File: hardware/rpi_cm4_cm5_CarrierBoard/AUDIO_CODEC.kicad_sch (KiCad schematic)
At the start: 33 parts, among them J12 SJ-3523-SMT-TR, J13 SJ-3523-SMT-TR, J14 SJ-3523-SMT-TR, U34 SGTL5000XNBA3R2, U35 AP22913W6-7, U36 AP22913W6-7, U37 12MHz, X1 CMM-3729AT-42308-TR

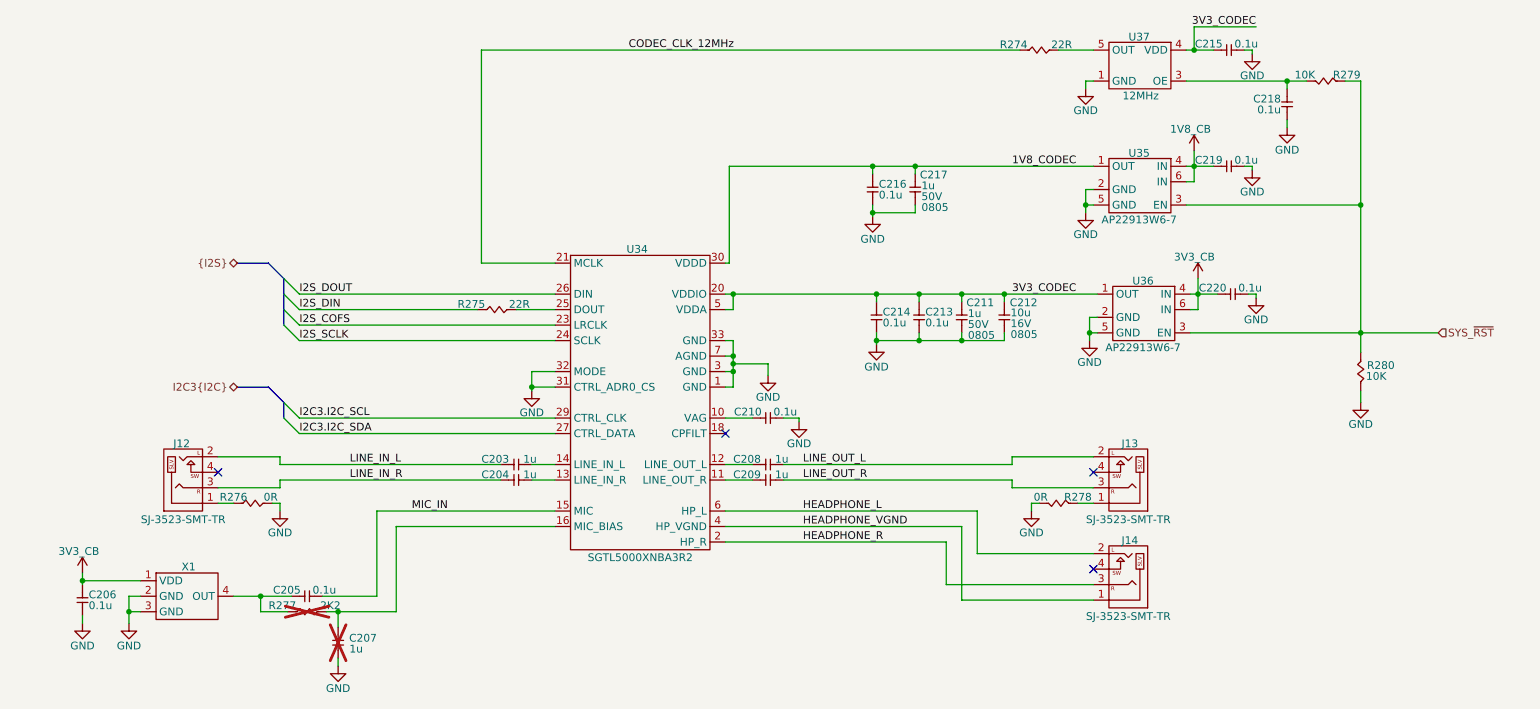
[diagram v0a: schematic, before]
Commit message: Preliminary completion of RPI CMx schematics Cleaned up hierarchical root page
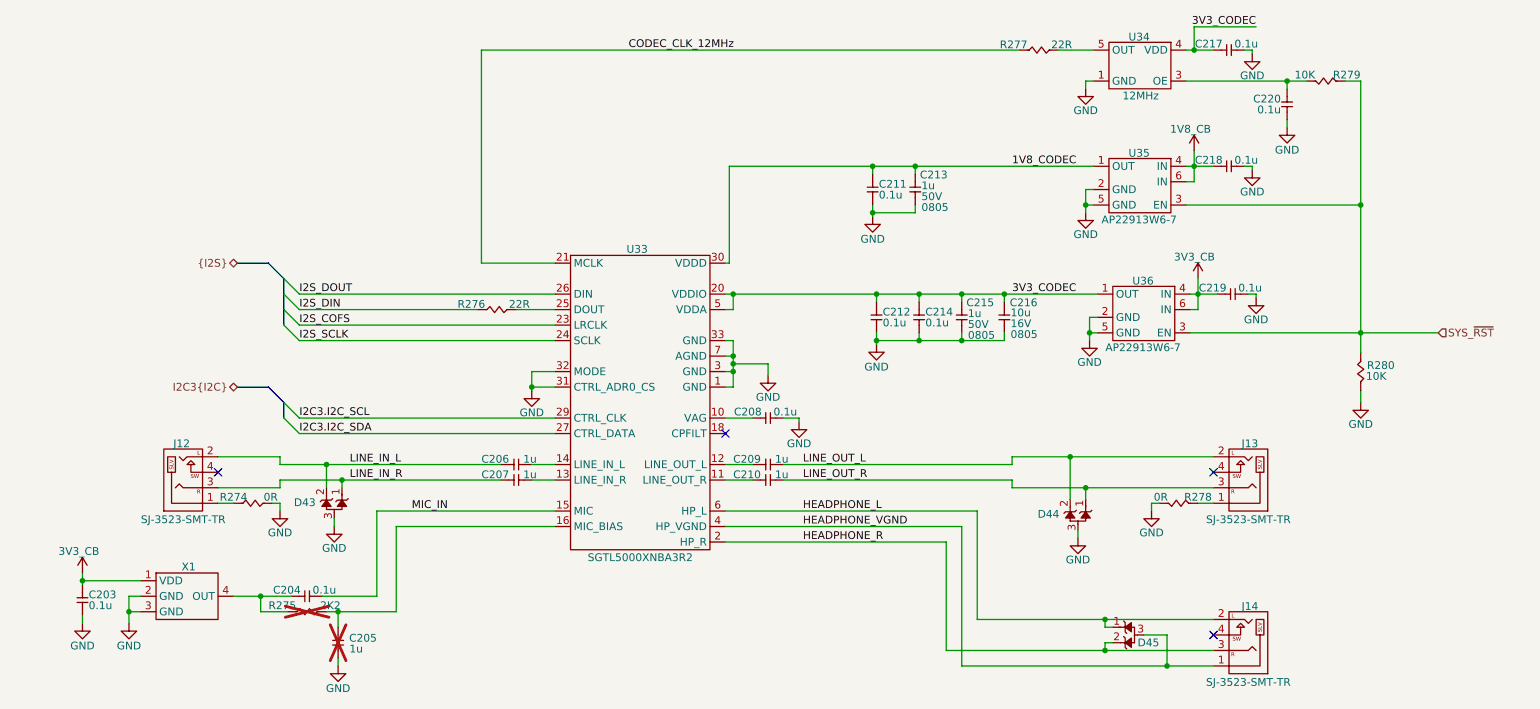
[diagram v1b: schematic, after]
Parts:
- added D43, D44, D45: D1213A-02SOL-7, footprint:SOT-23-3, symbol KicadCompDb:ESD Diodes/ESD_DIODE_00002
- renumbered C206 to C203, C205 to C204, C207 to C205, C203 to C206, C204 to C207, C210 to C208, C208 to C209, C209 to C210, C216 to C211, C214 to C212, C217 to C213, C213 to C214, C211 to C215, C212 to C216, C215 to C217, C219 to C218, C220 to C219, C218 to C220, R276 to R274, R277 to R275, R275 to R276, R274 to R277, U34 to U33, U37 to U34
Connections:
- net GND: now also D43.3 (GND), D44.3 (GND)
- net HEADPHONE_L: now also D45.1
- net HEADPHONE_R: now also D45.2 (A)
- net HEADPHONE_VGND: now also D45.3 (GND)
- net LINE_IN_L: now also D43.2 (A)
- net LINE_IN_R: now also D43.1
- net LINE_OUT_L: now also D44.2 (A)
- net LINE_OUT_R: now also D44.1
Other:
- moved on the sheet: J13, J14, R278

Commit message: Add preliminary BOM and preliminary .pdf schmematics Add BOM option for I2C control of ILI2132A for CapTouch HMI Add BOM options and DNP / 0R resistors for CM4 - CM5 build options
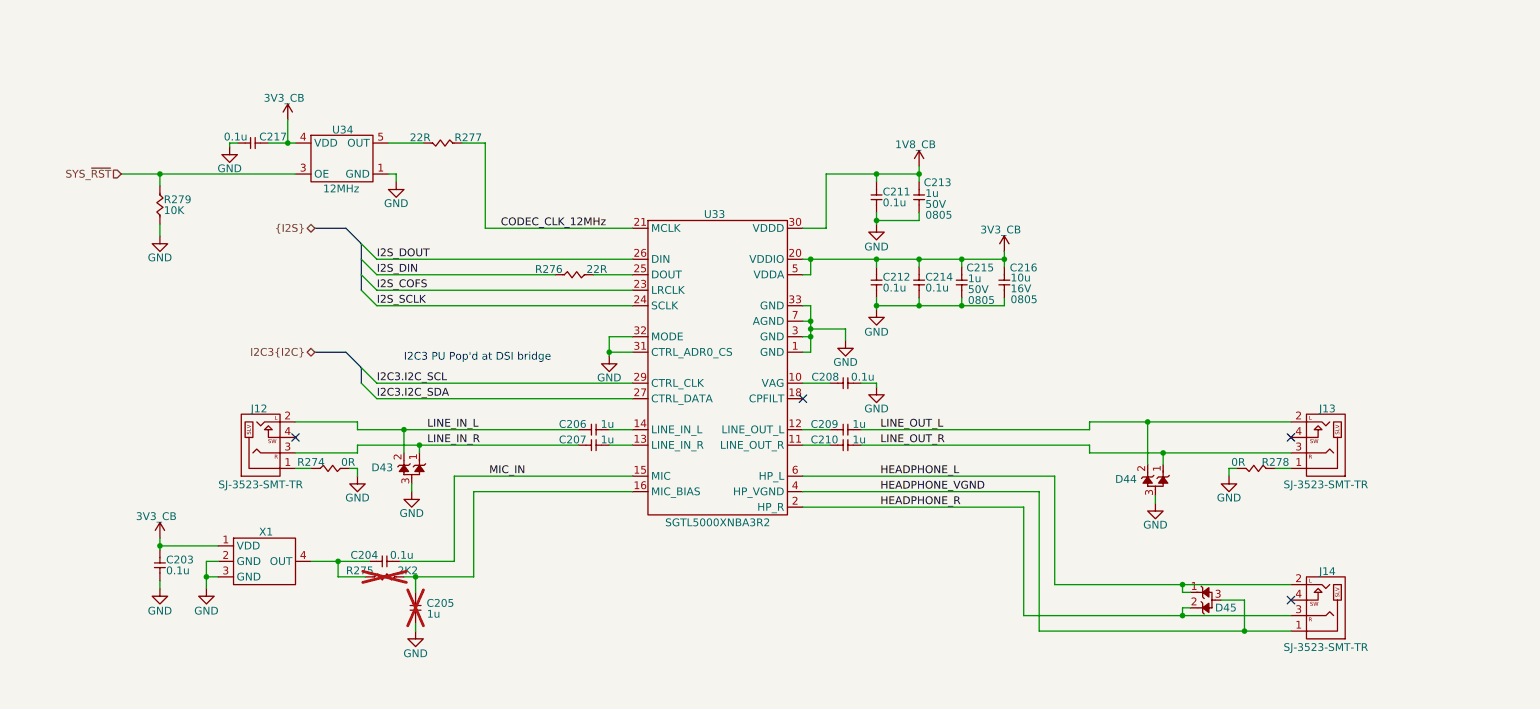
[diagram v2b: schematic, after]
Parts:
- removed C218, C219, C220: 0.1u, footprint:CAP_NONPOL_0402, symbol KicadCompDb:Capacitors/CAP_CER_SMT_00001
- removed R280: 10K, footprint:RES_0402, symbol KicadCompDb:Resistors/RES_SMT_00013
- removed U35, U36: AP22913W6-7, footprint:SOT-23-6, symbol KicadCompDb:Load Switch/LOAD_SW_00001
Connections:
- net 1V8_CODEC is gone; now on net 1V8_CB: C211.2, C213.2, U33.30 (VDDD)
- net 3V3_CODEC is gone; now on net 3V3_CB: C212.2, C214.2, C215.2, C216.2, C217.2, U33.20 (VDDIO), U33.5 (VDDA), U34.4 (VDD)
- net GND: now also R279.1
- net SYS_~{RST}: now also R279.2, U34.3 (OE); no longer R279.1
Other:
- note added: "I2C3 PU Pop'd at DSI bridge"
- moved on the sheet: C203, C204, C205, C206, C207, C208, C209, C210, C211, C212, C213, C214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

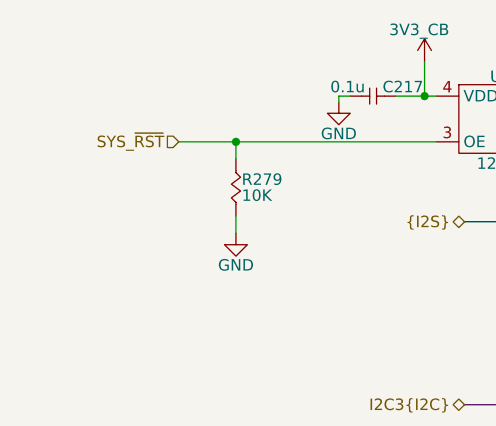
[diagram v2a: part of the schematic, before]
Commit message: Added power input protection & filter Added dedicated QWIIC connector on RPI CMx I2C6 bus Adjusted power table and PinMux Updated schematics accordingly
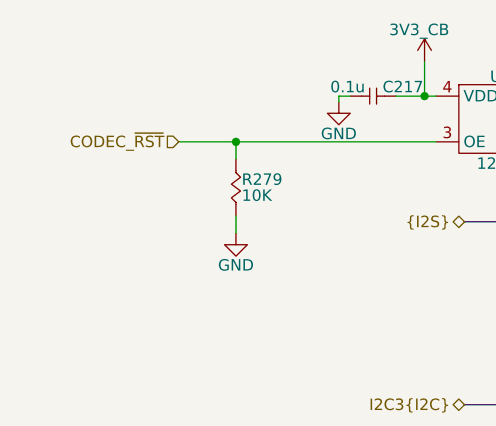
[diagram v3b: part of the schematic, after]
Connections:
- net SYS_~{RST} renamed CODEC_~{RST}
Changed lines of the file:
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@@
 		)
 	)
-	(hierarchical_label "SYS_~{RST}"
+	(hierarchical_label "CODEC_~{RST}"
 		(shape input)
 		(at 53.34 60.325 180)

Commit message: Update watchdog timer circuit to add external watchdog timer IC to be fed by PIC Adjust reset scheme in power supply sheet accordingly Adjust PinMux, regen BOM and PDF schematics (preliminary) Start preliminary component placement in the PCB
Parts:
- removed D43: D1213A-02SOL-7, footprint:SOT-23-3, symbol KicadCompDb:ESD Diodes/ESD_DIODE_00002
- removed J12: SJ-3523-SMT-TR, footprint:SJ-352X-SMT, symbol KicadCompDb:Connector/CONN_00013
- removed R274: 0R, footprint:RES_0402, symbol KicadCompDb:Resistors/RES_SMT_00001
- added R16, R17: 10K, footprint:RES_0402, symbol KicadCompDb:Resistors/RES_SMT_00013
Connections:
- net GND: now also R16.1, R17.1
- net LINE_IN_L: now also R17.2
- net LINE_IN_R: now also R16.2
- no-connect marks 4 -> 3
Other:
- moved on the sheet: C206, C207

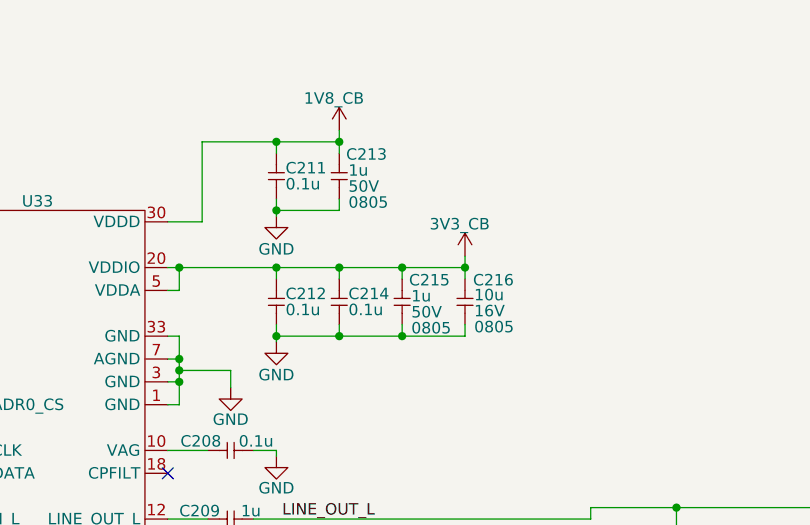
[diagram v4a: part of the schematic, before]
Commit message: Update preliminary placement, update DNP, regen BOM + Preliminary schematics
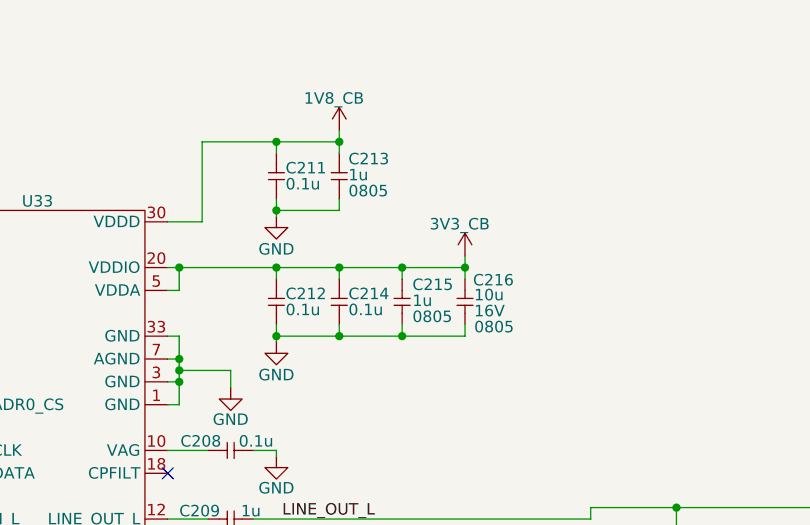
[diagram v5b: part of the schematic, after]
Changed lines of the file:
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@@
 		(dnp no)
 		(property "Reference" "C213"
-			(at 184.912 61.722 90)
+			(at 185.166 62.23 90)
 			(effects
 				(font
@@
 		)
 		(property "Value" "1u"
-			(at 185.166 63.5 90)
+			(at 185.166 64.008 90)
 			(effects
 				(font
@@
 		)
 		(property "Package" "0805"
-			(at 185.166 67.056 90)
+			(at 185.166 65.786 90)
 			(effects
 				(font
@@
 				)
 				(justify right)
+				(hide yes)
 			)
 		)
@@
 		(dnp no)
 		(property "Reference" "C215"
-			(at 191.897 75.692 90)
+			(at 192.278 76.2 90)
 			(effects
 				(font
@@
 		)
 		(property "Value" "1u"
-			(at 192.151 77.47 90)
+			(at 192.278 77.978 90)
 			(effects
 				(font
@@
 		)
 		(property "Package" "0805"
-			(at 192.151 81.026 90)
+			(at 192.278 79.756 90)
 			(effects
 				(font
@@
 				)
 				(justify right)
-			)
-		)
+				(hide yes)
+			)
+		)

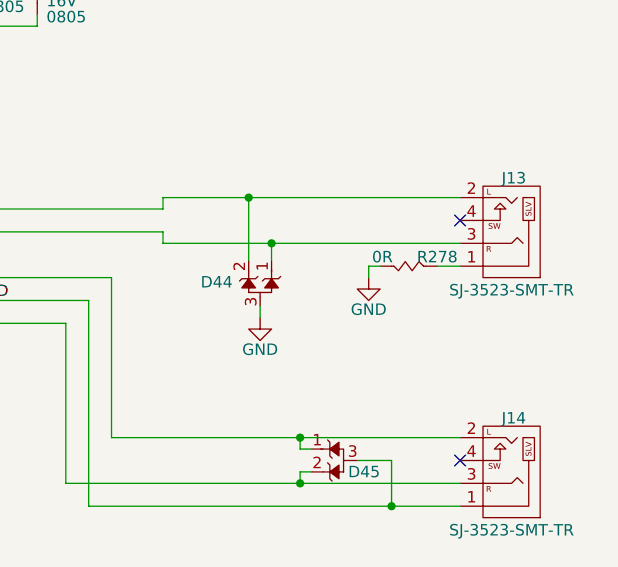
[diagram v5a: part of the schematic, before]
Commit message: Update PCB design rules for outer layers differential pairs Update preliminary component placement Update schematics based on PCB placement & remove duplicata / unnecessary components Update design notes and power table
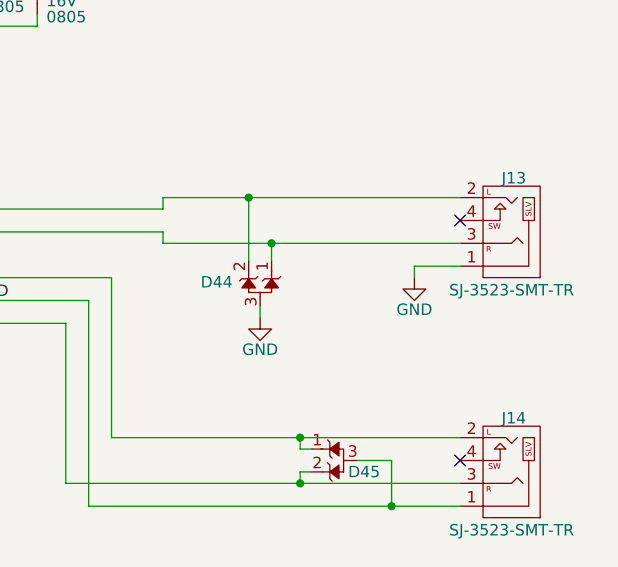
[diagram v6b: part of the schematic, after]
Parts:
- removed R278: 0R, footprint:RES_0402, symbol KicadCompDb:Resistors/RES_SMT_00001
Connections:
- net GND: now also J13.1 (SLV)
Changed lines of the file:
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@@
 	(wire
 		(pts
-			(xy 236.22 108.585) (xy 234.95 108.585)
+			(xy 240.03 108.585) (xy 245.11 108.585)
 		)
 		(stroke
@@
 	(wire
 		(pts
-			(xy 234.95 108.585) (xy 234.95 109.855)
+			(xy 240.03 108.585) (xy 240.03 109.855)
 		)
 		(stroke
@@
 	(wire
 		(pts
-			(xy 245.11 108.585) (xy 242.57 108.585)
-		)
-		(stroke
-			(width 0)
-			(type default)
-		)
-	)
-	(wire
-		(pts
 			(xy 201.295 114.935) (xy 201.295 132.715)
 		)
@@
 	)
 	(symbol
-		(lib_id "KicadCompDb:Resistors/RES_SMT_00001")
-		(at 241.3 108.585 0)
-		(mirror y)
-		(unit 1)
-		(exclude_from_sim no)
-		(in_bom yes)
-		(on_board yes)
-		(dnp no)
-		(property "Reference" "R278"
-			(at 242.57 107.569 0)
-			(effects
-				(font
-					(size 1.27 1.27)
-				)
-			)
-		)
-		(property "Value" "0R"
-			(at 236.474 107.569 0)
-			(effects
-				(font
-					(size 1.27 1.27)
-				)
-			)
-		)
-		(property "Footprint" "footprint:RES_0402"
-			(at 240.792 130.683 0)
-			(effects
-				(font
-					(size 1.27 1.27)
-				)
-				(hide yes)
-			)
-		)
-		(property "Datasheet" "https://www.yageogroup.com/content/datasheet/asset/file/PYU-RC_GROUP_51_ROHS_L"
-			(at 241.3 108.585 0)
-			(effects
-				(font
-					(size 1.27 1.27)
-				)
-				(hide yes)
-			)
-		)
-		(property "Description" "RES 0 OHM JUMPER 1/16W 0402"
-			(at 239.522 118.491 0)
-			(effects
-				(font
-					(size 1.27 1.27)
-				)
-				(hide yes)
-			)
-		)
-		(property "Tolerance" "1%"
-			(at 241.046 128.905 0)
-			(effects
-				(font
-					(size 1.27 1.27)
-				)
-				(hide yes)
-			)
-		)
-		(property "Power" "1/16W"
-			(at 241.046 122.809 0)
-			(effects
-				(font
-					(size 1.27 1.27)
-				)
-				(hide yes)
-			)
-		)
-		(property "Package" "0402"
-			(at 241.3 124.841 0)
-			(effects
-				(font
-					(size 1.27 1.27)
-				)
-				(hide yes)
-			)
-		)
-		(property "Manufacturer" "YAGEO"
-			(at 241.046 126.873 0)
-			(effects
-				(font
-					(size 1.27 1.27)
-				)
-				(hide yes)
-			)
-		)
-		(property "Manufacturer Part Number" "RC0402FR-071KL"
-			(at 241.046 116.459 0)
-			(effects
-				(font
-					(size 1.27 1.27)
-				)
-				(hide yes)
-			)
-		)
-		(property "Distributor" "DigiKey"
-			(at 241.3 114.427 0)
-			(effects
-				(font
-					(size 1.27 1.27)
-				)
-				(hide yes)
-			)
-		)
-		(property "Distributor Part Number" "311-0.0JRCT-ND"
-			(at 240.538 120.777 0)
-			(effects
-				(font
-					(size 1.27 1.27)
-				)
-				(hide yes)
-			)
-		)
-		(property "Temperature Coefficient" "±100ppm/°C"
-			(at 241.3 108.585 0)
-			(effects
-				(font
-					(size 1.27 1.27)
-				)
-				(hide yes)
-			)
-		)
-		(property "Operating Temperature" "-55°C ~ 155°C"
-			(at 240.538 132.969 0)
-			(effects
-				(font
-					(size 1.27 1.27)
-				)
-				(hide yes)
-			)
-		)
-		(property "Type" "RES SMT"
-			(at 241.3 108.585 0)
-			(show_name yes)
-			(effects
-				(font
-					(size 1.27 1.27)
-				)
-				(hide yes)
-			)
-		)
-		(property "Dimensions" "1.00mm x 0.50mm"
-			(at 241.3 108.585 0)
-			(show_name yes)
-			(effects
-				(font
-					(size 1.27 1.27)
-				)
-				(hide yes)
-			)
-		)
-		(pin "1"
-		)
-		(pin "2"
-		)
-		(instances
-			(project "rpi_cm4_cm5_CarrierBoard"
-				(path "/7dcdf741-90ca-4333-848c-806f4d64158e/6be3aa9b-6529-4327-ac7b-64810effdbd4"
-					(reference "R278")
-					(unit 1)
-				)
-			)
-		)
-	)
-	(symbol
 		(lib_id "KicadCompDb:Resistors/RES_SMT_00015")
 		(at 104.14 55.245 0)
@@
 	(symbol
 		(lib_id "KiCad_Pwr_Symbols:GND")
-		(at 234.95 109.855 0)
+		(at 240.03 109.855 0)
 		(mirror y)
 		(unit 1)
@@
 		(dnp no)
 		(property "Reference" "#PWR0340"
-			(at 234.95 116.205 0)
+			(at 240.03 116.205 0)
 			(effects
 				(font
@@
 		)
 		(property "Value" "GND"
-			(at 234.95 113.411 0)
+			(at 240.03 113.411 0)
 			(effects
 				(font
@@
 		)
 		(property "Footprint" ""
-			(at 234.95 109.855 0)
+			(at 240.03 109.855 0)
 			(effects
 				(font
@@
 		)
 		(property "Datasheet" ""
-			(at 234.95 109.855 0)
+			(at 240.03 109.855 0)
 			(effects
 				(font
@@
 		)
 		(property "Description" "Power symbol creates a global label with name \"GND\" , ground"
-			(at 234.95 109.855 0)
+			(at 240.03 109.855 0)
 			(effects
 				(font
